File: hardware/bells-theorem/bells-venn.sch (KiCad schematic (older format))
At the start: 0 parts

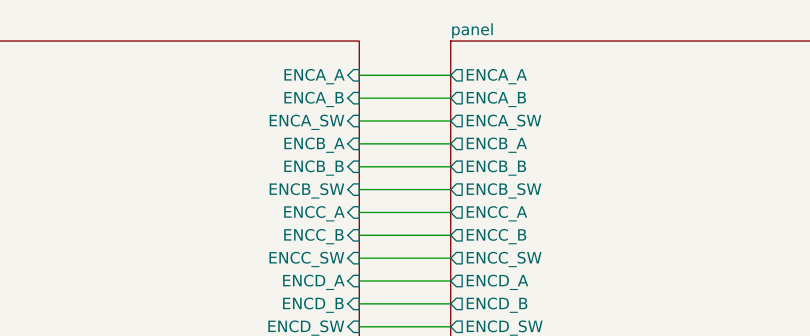
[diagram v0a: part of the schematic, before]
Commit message: version 0.3, update for corrected LED drivers, other tweaks
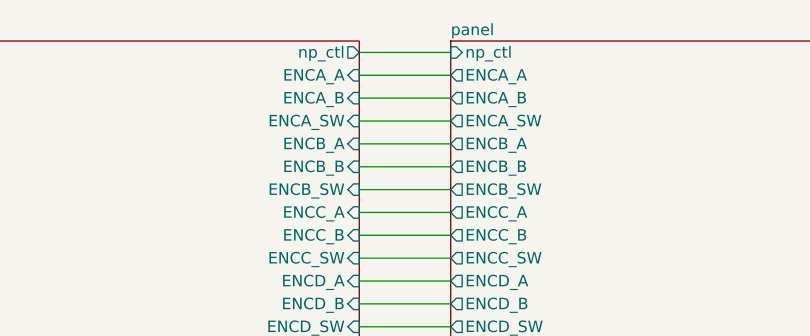
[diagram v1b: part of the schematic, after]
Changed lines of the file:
@@
 F30 "DAB" I L 6500 4000 50
 F31 "ABCD" I L 6500 4100 50
+F32 "np_ctl" I L 6500 1500 50
 $EndSheet
 Wire Wire Line
@@
 F30 "ENCB_SW" I R 6100 2100 50
 F31 "ENCB_B" I R 6100 2000 50
+F32 "np_ctl" O R 6100 1500 50
 $EndSheet
+Wire Wire Line
+	6100 1500 6500 1500
 $EndSCHEMATC
